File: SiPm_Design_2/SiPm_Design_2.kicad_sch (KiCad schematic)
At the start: 18 parts, among them IC1 OPA354AIDDAR, IC2 OPA354AIDDAR, IC3 OPA354AIDDAR, IC4 AFBR-S4N44P014M

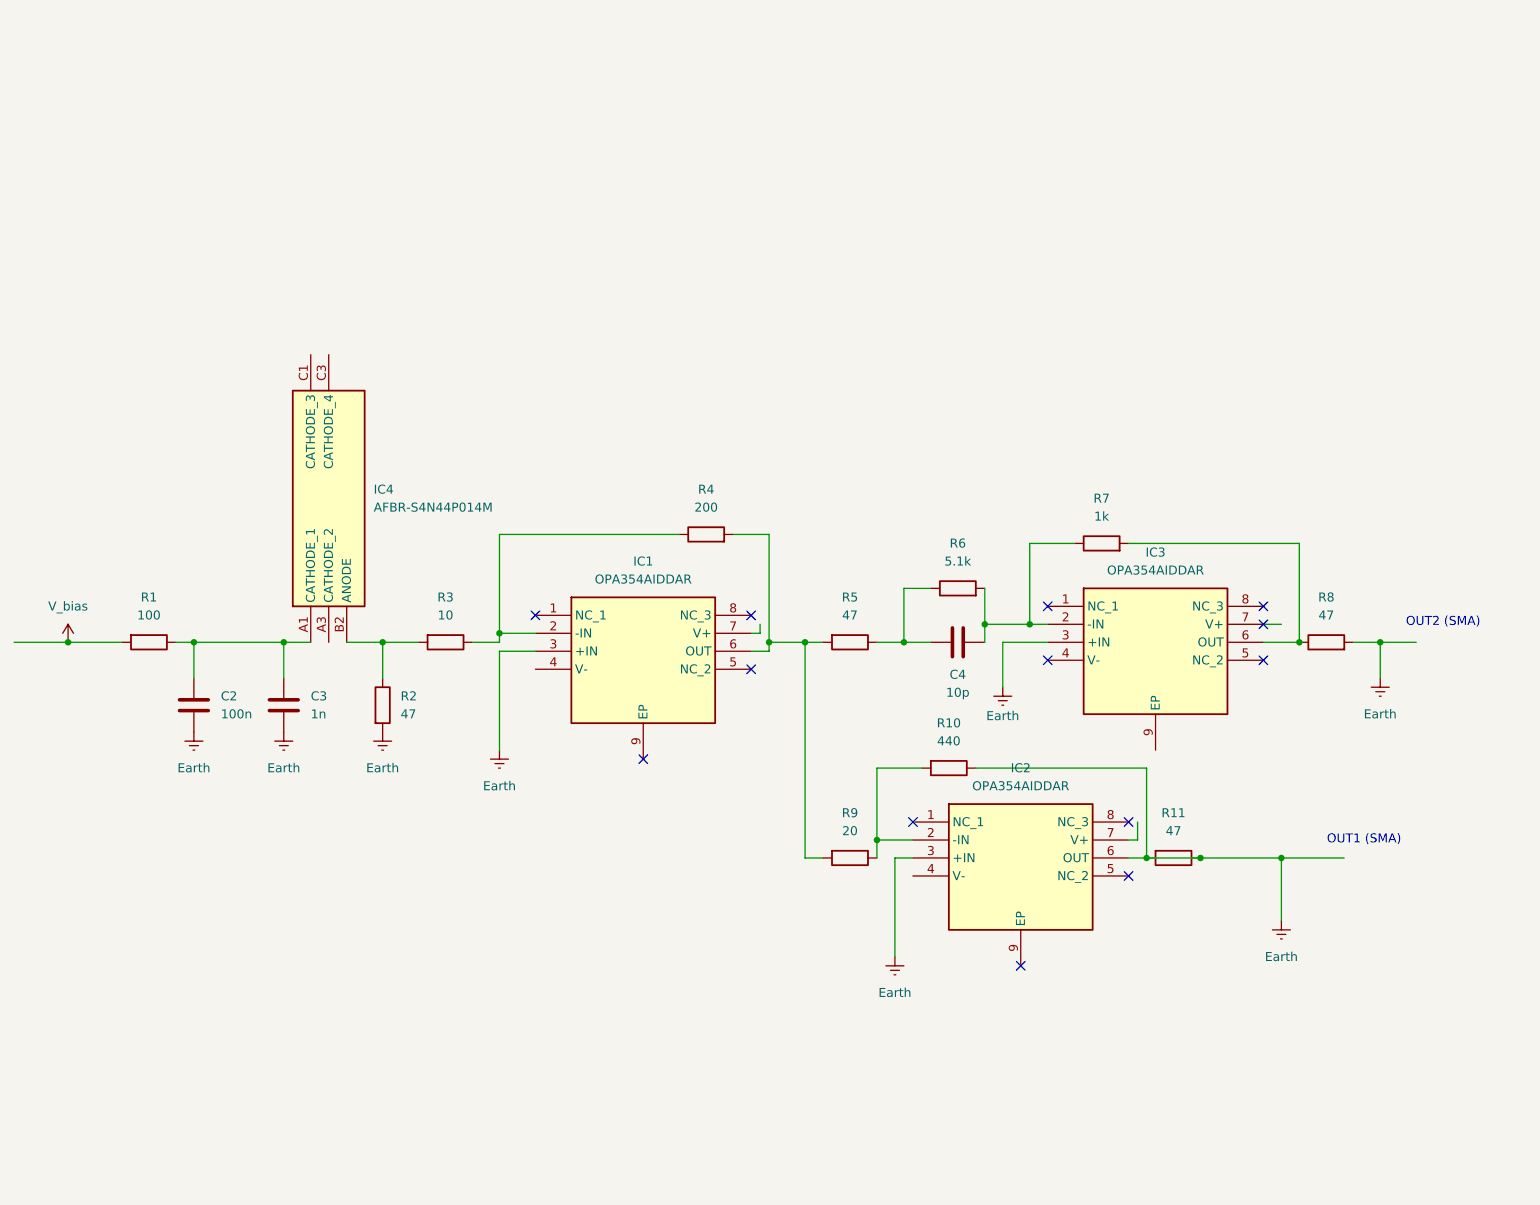
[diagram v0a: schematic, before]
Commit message: add +/- 2.5V "bypass cap"
add +/- 2.5V "bypass cap"
add res to V+ input
add feedback cap
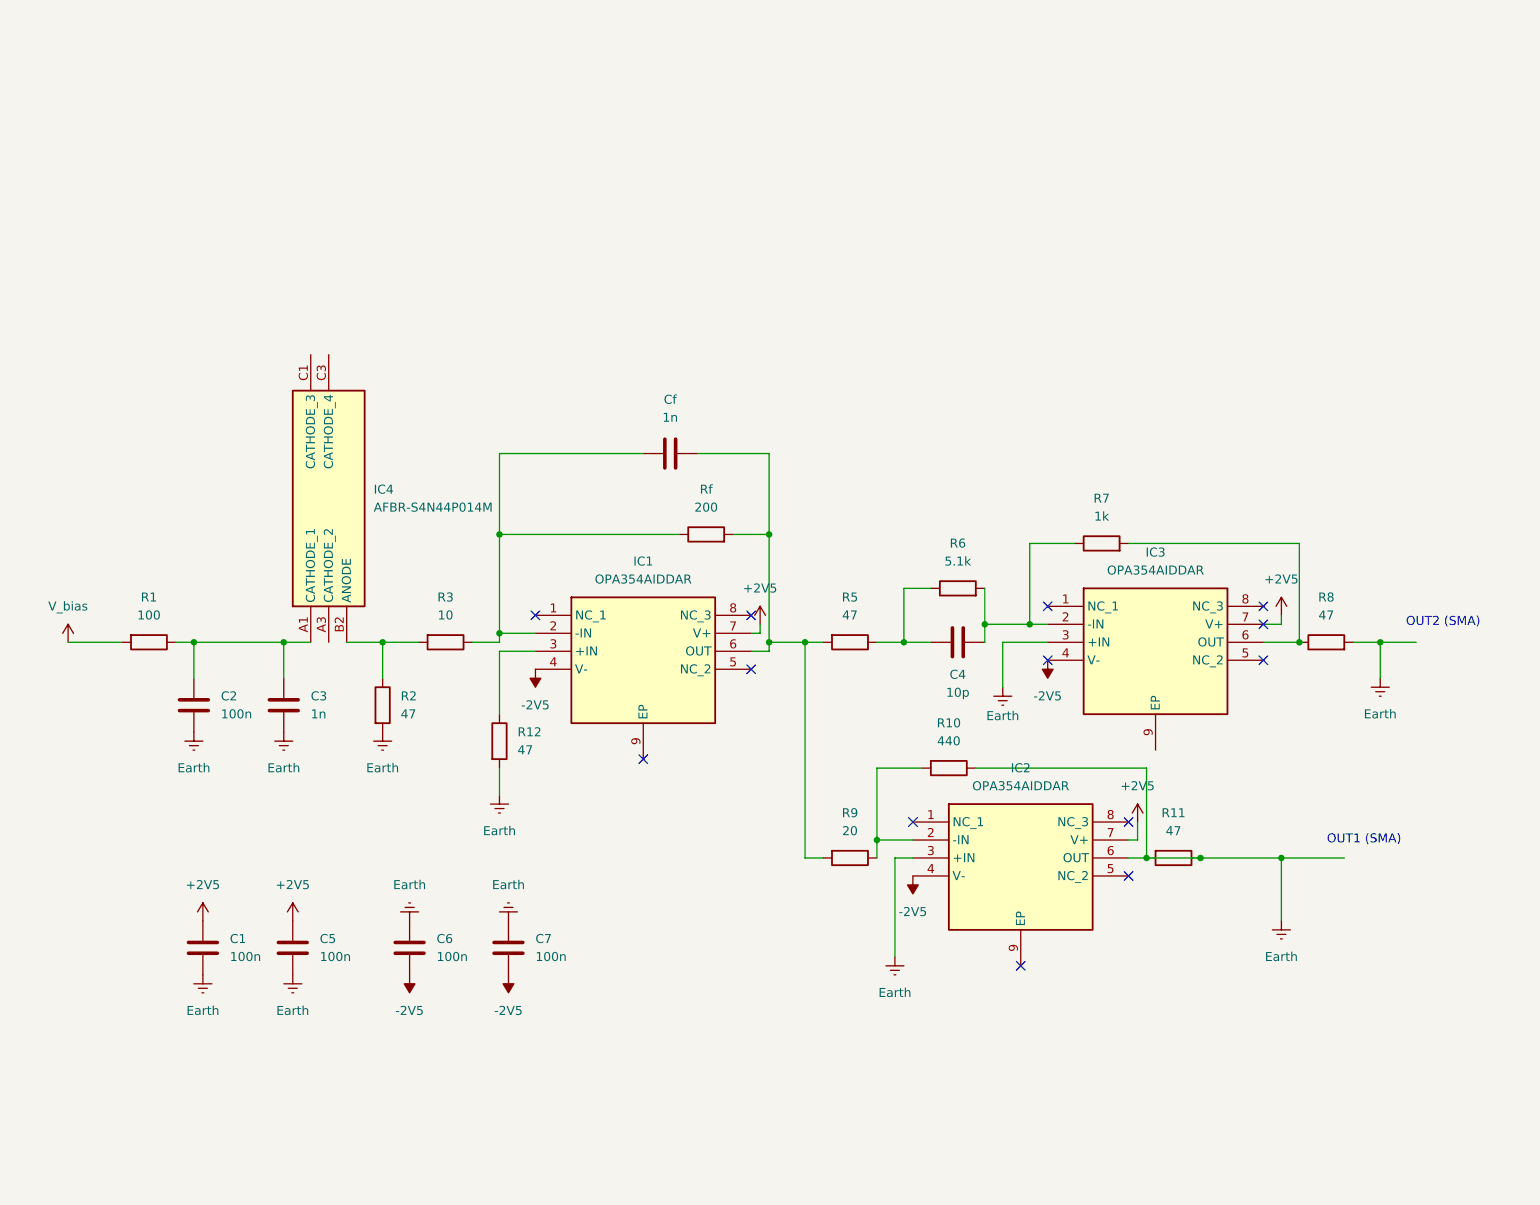
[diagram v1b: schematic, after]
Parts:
- added C1, C5, C6, C7: 100n, Capacitor_Tantalum_SMD:CP_EIA-2012-12_Kemet-R_Pad1.30x1.05mm_HandSolder, symbol Device:C
- added Cf: 1n, Capacitor_Tantalum_SMD:CP_EIA-2012-12_Kemet-R_Pad1.30x1.05mm_HandSolder, symbol Device:C
- added R12: 47, Resistor_SMD:R_1812_4532Metric_Pad1.30x3.40mm_HandSolder, symbol Device:R
- renumbered R4 to Rf
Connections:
- net Earth: now also C1.2, C5.2, C6.1, C7.1, R12.2; no longer IC1.3 (+IN)
- net at IC1.2 (-IN), R3.1, Rf.1: now also Cf.1
- net -2V5: now reaches IC1.4 (V-)
- net -2V5: now also IC2.4 (V-), IC3.4 (V-), C6.2, C7.2
- net at IC1.6 (OUT), R5.2, R9.2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: now also Cf.2
- net +2V5: now reaches IC1.7 (V+)
- net +2V5: now also IC2.7 (V+), IC3.7 (V+), C1.1, C5.1
- new net: IC1.3 (+IN), R12.1

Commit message: change footprint of some res cap
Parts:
- C1, C2, C3, C5, C6, C7: footprint Capacitor_Tantalum_SMD:CP_EIA-2012-12_Kemet-R_Pad1.30x1.05mm_HandSolder -> Capacitor_SMD:C_0603_1608Metric_Pad1.08x0.95mm_HandSolder
- Cf1: renamed from Cf; footprint Capacitor_Tantalum_SMD:CP_EIA-2012-12_Kemet-R_Pad1.30x1.05mm_HandSolder -> Capacitor_SMD:C_0603_1608Metric_Pad1.08x0.95mm_HandSolder
- IC1, IC2, IC3: footprint SOIC127P600X170-9N -> Package_SO:HSOP-8-1EP_3.9x4.9mm_P1.27mm_EP2.3x2.3mm
- IC4: footprint AFBRS4N44P014M -> S4N44P014M:AFBRS4N44P014M
- R12, R3: footprint Resistor_SMD:R_1812_4532Metric_Pad1.30x3.40mm_HandSolder -> Resistor_SMD:R_0603_1608Metric_Pad0.98x0.95mm_HandSolder
- Rf1: renamed from Rf; footprint Resistor_SMD:R_1812_4532Metric_Pad1.30x3.40mm_HandSolder -> Resistor_SMD:R_0603_1608Metric_Pad0.98x0.95mm_HandSolder
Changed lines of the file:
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@@
 			)
 		)
-		(property "Footprint" "Capacitor_Tantalum_SMD:CP_EIA-2012-12_Kemet-R_Pad1.30x1.05mm_HandSolder"
+		(property "Footprint" "Capacitor_SMD:C_0603_1608Metric_Pad1.08x0.95mm_HandSolder"
 			(at 84.7852 114.3 0)
 			(effects
@@
 			)
 		)
-		(property "Footprint" "Capacitor_Tantalum_SMD:CP_EIA-2012-12_Kemet-R_Pad1.30x1.05mm_HandSolder"
+		(property "Footprint" "Capacitor_SMD:C_0603_1608Metric_Pad1.08x0.95mm_HandSolder"
 			(at 129.2352 148.59 0)
 			(effects
@@
 			)
 		)
-		(property "Footprint" "Resistor_SMD:R_1812_4532Metric_Pad1.30x3.40mm_HandSolder"
+		(property "Footprint" "Resistor_SMD:R_0603_1608Metric_Pad0.98x0.95mm_HandSolder"
 			(at 119.38 99.822 90)
 			(effects
@@
 			)
 		)
-		(property "Footprint" "SOIC127P600X170-9N"
+		(property "Footprint" "Package_SO:HSOP-8-1EP_3.9x4.9mm_P1.27mm_EP2.3x2.3mm"
 			(at 158.75 192.71 0)
 			(effects
@@
 			)
 		)
-		(property "Footprint" "AFBRS4N44P014M"
+		(property "Footprint" "S4N44P014M:AFBRS4N44P014M"
 			(at 195.25 64.77 0)
 			(effects
@@
 			)
 		)
-		(property "Footprint" "Capacitor_Tantalum_SMD:CP_EIA-2012-12_Kemet-R_Pad1.30x1.05mm_HandSolder"
+		(property "Footprint" "Capacitor_SMD:C_0603_1608Metric_Pad1.08x0.95mm_HandSolder"
 			(at 115.2652 148.59 0)
 			(effects
@@
 		(dnp no)
 		(fields_autoplaced yes)
-		(property "Reference" "Rf"
+		(property "Reference" "Rf1"
 			(at 156.21 80.01 90)
 			(effects
@@
 			)
 		)
-		(property "Footprint" "Resistor_SMD:R_1812_4532Metric_Pad1.30x3.40mm_HandSolder"
+		(property "Footprint" "Resistor_SMD:R_0603_1608Metric_Pad0.98x0.95mm_HandSolder"
 			(at 156.21 88.138 90)
 			(effects
@@
 			(project ""
 				(path "/d64cfca3-4032-4a91-b47d-ee8cac34c76a"
-					(reference "Rf")
+					(reference "Rf1")
 					(unit 1)
 				)
@@
 			)
 		)
-		(property "Footprint" "Capacitor_Tantalum_SMD:CP_EIA-2012-12_Kemet-R_Pad1.30x1.05mm_HandSolder"
+		(property "Footprint" "Capacitor_SMD:C_0603_1608Metric_Pad1.08x0.95mm_HandSolder"
 			(at 98.7552 148.59 0)
 			(effects
@@
 			)
 		)
-		(property "Footprint" "Capacitor_Tantalum_SMD:CP_EIA-2012-12_Kemet-R_Pad1.30x1.05mm_HandSolder"
+		(property "Footprint" "Capacitor_SMD:C_0603_1608Metric_Pad1.08x0.95mm_HandSolder"
 			(at 86.0552 148.59 0)
 			(effects
@@
 		(dnp no)
 		(fields_autoplaced yes)
-		(property "Reference" "Cf"
+		(property "Reference" "Cf1"
 			(at 151.13 67.31 90)
 			(effects
@@
 			)
 		)
-		(property "Footprint" "Capacitor_Tantalum_SMD:CP_EIA-2012-12_Kemet-R_Pad1.30x1.05mm_HandSolder"
+		(property "Footprint" "Capacitor_SMD:C_0603_1608Metric_Pad1.08x0.95mm_HandSolder"
 			(at 154.94 73.9648 0)
 			(effects
@@
 			(project "SiPm_Design_2"
 				(path "/d64cfca3-4032-4a91-b47d-ee8cac34c76a"
-					(reference "Cf")
+					(reference "Cf1")
 					(unit 1)
 				)
@@
 			)
 		)
-		(property "Footprint" "Resistor_SMD:R_1812_4532Metric_Pad1.30x3.40mm_HandSolder"
+		(property "Footprint" "Resistor_SMD:R_0603_1608Metric_Pad0.98x0.95mm_HandSolder"
 			(at 125.222 115.57 90)
 			(effects
@@
 			)
 		)
-		(property "Footprint" "SOIC127P600X170-9N"
+		(property "Footprint" "Package_SO:HSOP-8-1EP_3.9x4.9mm_P1.27mm_EP2.3x2.3mm"
 			(at 231.14 191.44 0)
 			(effects
@@
 			)
 		)
-		(property "Footprint" "Capacitor_Tantalum_SMD:CP_EIA-2012-12_Kemet-R_Pad1.30x1.05mm_HandSolder"
+		(property "Footprint" "Capacitor_SMD:C_0603_1608Metric_Pad1.08x0.95mm_HandSolder"
 			(at 97.4852 114.3 0)
 			(effects
@@
 			)
 		)
-		(property "Footprint" "SOIC127P600X170-9N"
+		(property "Footprint" "Package_SO:HSOP-8-1EP_3.9x4.9mm_P1.27mm_EP2.3x2.3mm"
 			(at 212.09 221.92 0)
 			(effects

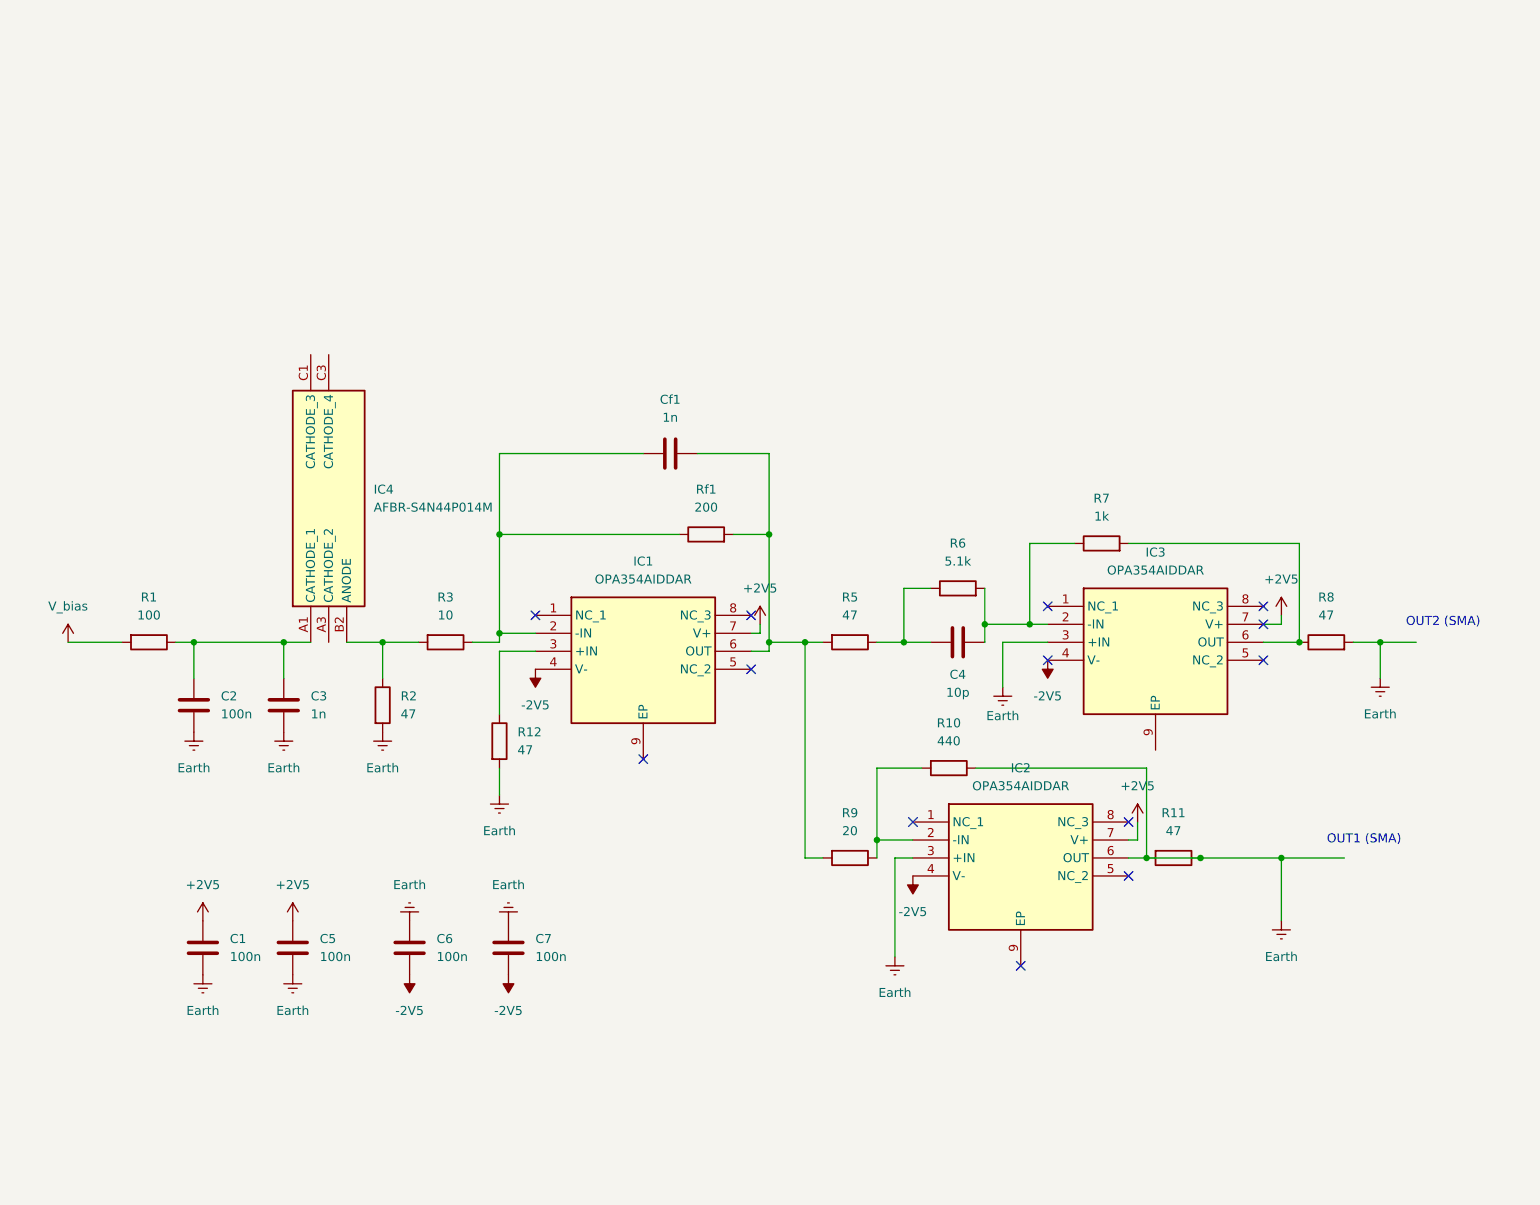
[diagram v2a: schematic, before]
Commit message: change to 2 opamp
add connector
change to OPA2354
done layout as 2 layers
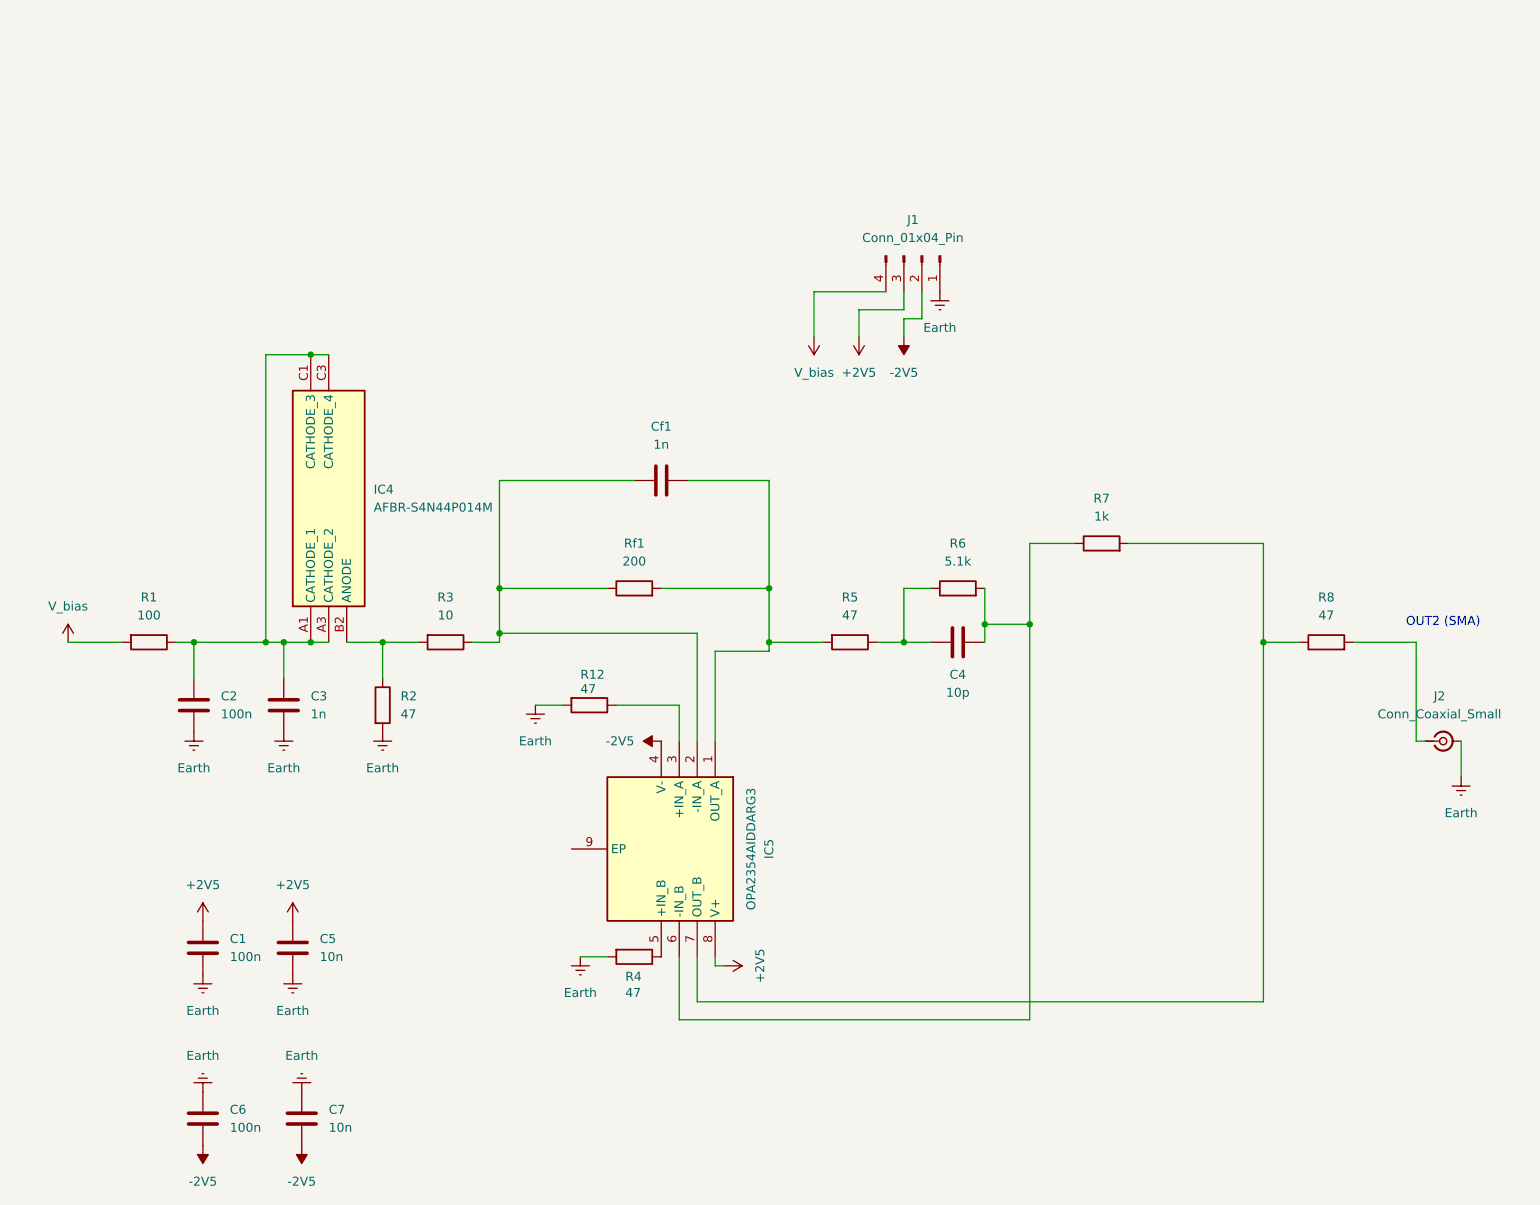
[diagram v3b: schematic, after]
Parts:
- removed IC1, IC2, IC3: OPA354AIDDAR, Package_SO:HSOP-8-1EP_3.9x4.9mm_P1.27mm_EP2.3x2.3mm, symbol OPA354AIDDAR:OPA354AIDDAR
- removed R10: 440, Resistor_SMD:R_1812_4532Metric_Pad1.30x3.40mm_HandSolder, symbol Device:R
- removed R11: 47, Resistor_SMD:R_1812_4532Metric_Pad1.30x3.40mm_HandSolder, symbol Device:R
- removed R9: 20, Resistor_SMD:R_1812_4532Metric_Pad1.30x3.40mm_HandSolder, symbol Device:R
- added IC5: OPA2354AIDDARG3, LIB_OPA2354AIDDARG3:SOIC127P600X170-9N, symbol OPA2354AIDDARG3:OPA2354AIDDARG3
- added J1: Conn_01x04_Pin, Connector_Molex:Molex_KK-396_A-41792-0004_1x04_P3.96mm_Horizontal, symbol Connector:Conn_01x04_Pin
- added J2: Conn_Coaxial_Small, Connector_Coaxial:SMA_Amphenol_901-143_Horizontal, symbol Connector:Conn_Coaxial_Small
- added R4: 47, Resistor_SMD:R_0603_1608Metric_Pad0.98x0.95mm_HandSolder, symbol Device:R
- C4: footprint Capacitor_Tantalum_SMD:CP_EIA-2012-12_Kemet-R_Pad1.30x1.05mm_HandSolder -> Capacitor_SMD:C_0603_1608Metric_Pad1.08x0.95mm_HandSolder
- C5, C7: value 100n -> 10n
- R1, R2, R5, R6, R7, R8: footprint Resistor_SMD:R_1812_4532Metric_Pad1.30x3.40mm_HandSolder -> Resistor_SMD:R_0603_1608Metric_Pad0.98x0.95mm_HandSolder
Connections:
- net +2V5: now also IC5.8 (V+), J1.3 (Pin_3)
- net -2V5: now also IC5.4 (V-), J1.2 (Pin_2)
- net Earth: now also J1.1 (Pin_1), J2.2 (Ext), R4.2; no longer R8.2
- net V_bias: now also J1.4 (Pin_4)
- net at C4.2, R6.2, R7.1: now also IC5.6 (-IN_B)
- net at R7.2, R8.1: now also IC5.7 (OUT_B)
- net at C2.1, C3.1, IC4.A1 (CATHODE_1)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: now also IC4.A3 (CATHODE_2), IC4.C1 (CATHODE_3), IC4.C3 (CATHODE_4)
- net at Cf1.1, R3.1, Rf1.1: now also IC5.2 (-IN_A)
- net at R12.1: now also IC5.3 (+IN_A)
- net at Cf1.2, R5.2, Rf1.2: now also IC5.1 (OUT_A)
- new net: J2.1 (In), R8.2
- new net: IC5.5 (+IN_B), R4.1
- no-connect marks 13 -> 0
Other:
- note removed: "OUT1 (SMA)"
- moved on the sheet: C6, C7, Cf1, R12, Rf1
